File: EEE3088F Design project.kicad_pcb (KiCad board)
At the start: 2 copper layers, 2 parts, among them U7 INA219AxD

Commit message: added circuits
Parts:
- added R9: 1206W4F1002T5E, Resistor_SMD:R_1206_3216Metric_Pad1.30x1.75mm_HandSolder, F.Cu at (148.4, 91.5)

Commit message: saved PCB
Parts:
- added C8: 1uF, Capacitor_SMD:C_1206_3216Metric_Pad1.33x1.80mm_HandSolder, F.Cu at (120.9, 124.9)
- added C9: 1uF, Capacitor_SMD:C_1206_3216Metric_Pad1.33x1.80mm_HandSolder, F.Cu at (129.3, 109.5)
- added D1: D_Schottky, Diode_SMD:D_SOD-123, F.Cu at (126.8, 124.9)
- added D2: D_Schottky, Diode_SMD:D_SOD-123, F.Cu at (129.3, 112.9)
- added L1: 22uH, Inductor_SMD:L_0603_1608Metric_Pad1.05x0.95mm_HandSolder, F.Cu at (126.1, 127.8)
- added L2: 22uH, Inductor_SMD:L_0603_1608Metric_Pad1.05x0.95mm_HandSolder, F.Cu at (120.1, 113.4)
- added L3: 47uH, Inductor_SMD:L_0805_2012Metric_Pad1.05x1.20mm_HandSolder, F.Cu at (133.5, 100.4)
- added Q1: NMOS, Package_TO_SOT_SMD:SOT-23, F.Cu at (133.5, 104.1)
- added R10: 1.1k, Resistor_SMD:R_1206_3216Metric_Pad1.30x1.75mm_HandSolder, F.Cu at (140.9, 100.6)
- added R11: 68, Resistor_SMD:R_1206_3216Metric_Pad1.30x1.75mm_HandSolder, F.Cu at (140.9, 103.9)
- added R12: 1.1k, Resistor_SMD:R_1206_3216Metric_Pad1.30x1.75mm_HandSolder, F.Cu at (140.9, 107.2)
- added R13: 68, Resistor_SMD:R_1206_3216Metric_Pad1.30x1.75mm_HandSolder, F.Cu at (140.9, 110.5)
- added R14: 5.1k, Resistor_SMD:R_0805_2012Metric_Pad1.20x1.40mm_HandSolder, F.Cu at (128.7, 100.5)
- added R15: 390, Resistor_SMD:R_0805_2012Metric_Pad1.20x1.40mm_HandSolder, F.Cu at (128.7, 103.4)
- added R16: 2.7k, Resistor_SMD:R_0805_2012Metric_Pad1.20x1.40mm_HandSolder, F.Cu at (128.7, 106.4)
- added U4: XL1509-3.3, Package_SO:SOIC-8_3.9x4.9mm_P1.27mm, F.Cu at (122.1, 120.0)
- added U7: XL1509-5.0, Package_SO:SOIC-8_3.9x4.9mm_P1.27mm, F.Cu at (122.1, 102.3)
- added U8: TP4056-42-ESOP8, Package_SO:SOIC-8-1EP_3.9x4.9mm_P1.27mm_EP2.41x3.3mm_ThermalVias, F.Cu at (122.1, 108.9)

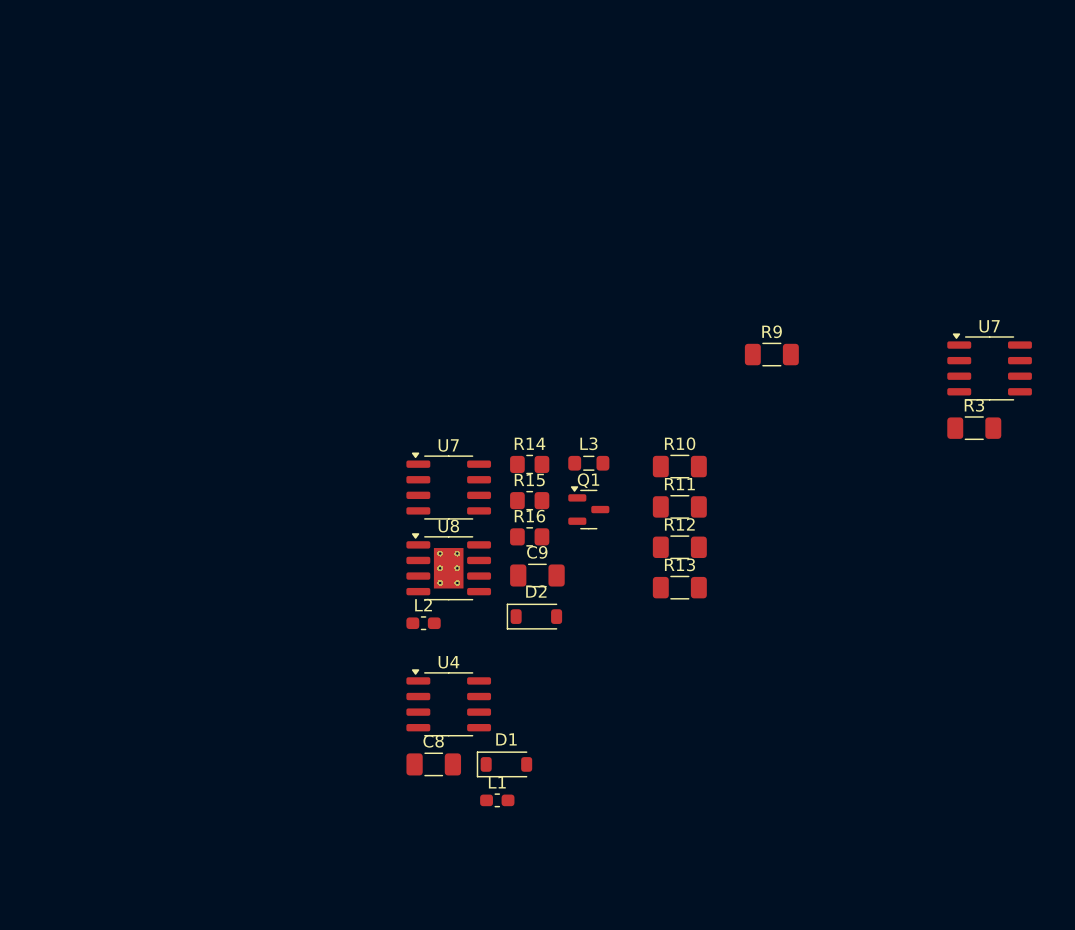
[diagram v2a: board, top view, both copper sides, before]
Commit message: added LCSC numbers and finsihed footprints
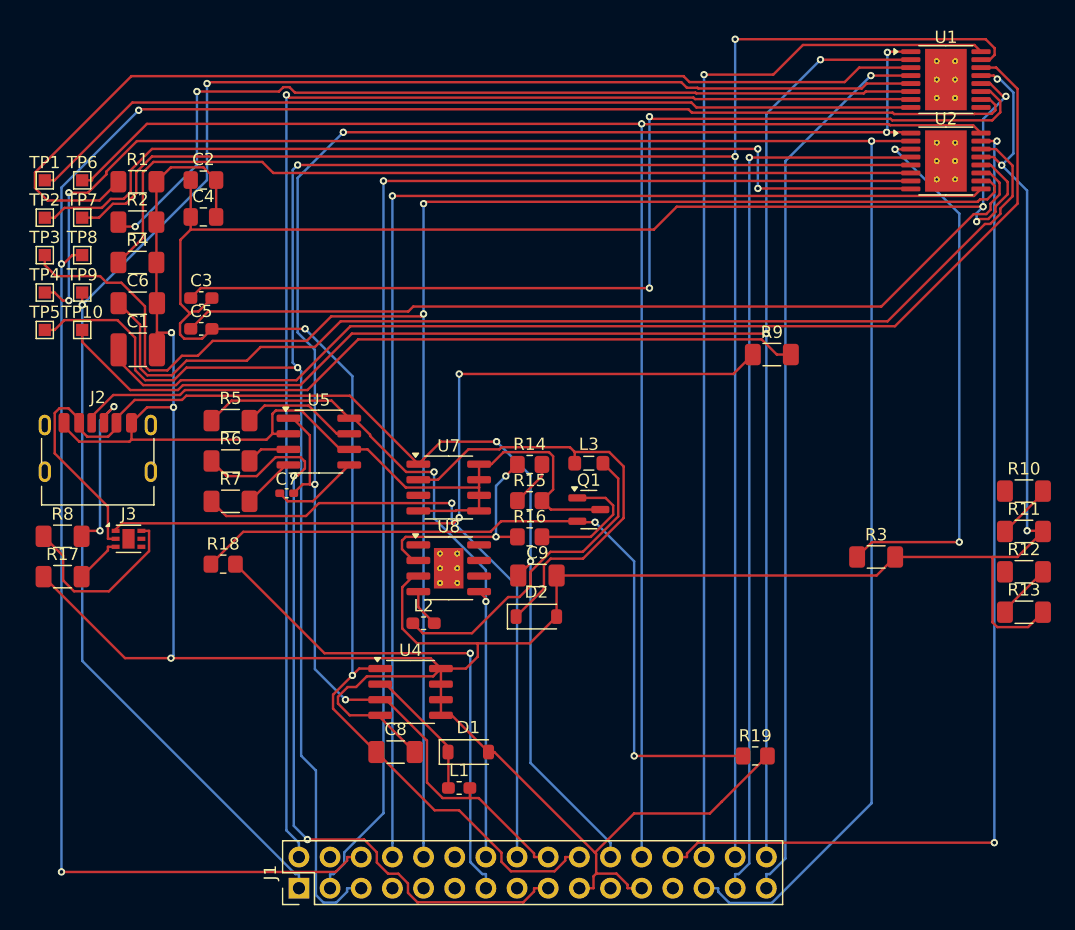
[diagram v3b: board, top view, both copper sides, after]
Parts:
- removed the U7 at (166.2, 92.6)
- added C1: 2.2μ, Capacitor_SMD:C_1210_3225Metric_Pad1.33x2.70mm_HandSolder, F.Cu at (96.8, 91.1)
- added C2: 10μ, Capacitor_SMD:C_0805_2012Metric_Pad1.18x1.45mm_HandSolder, F.Cu at (102.1, 77.3)
- added C3: 10n, Capacitor_SMD:C_0603_1608Metric_Pad1.08x0.95mm_HandSolder, F.Cu at (101.9, 86.9)
- added C4: 10μ, Capacitor_SMD:C_0805_2012Metric_Pad1.18x1.45mm_HandSolder, F.Cu at (102.1, 80.3)
- added C5: 10n, Capacitor_SMD:C_0603_1608Metric_Pad1.08x0.95mm_HandSolder, F.Cu at (101.9, 89.4)
- added C6: 2.2μ, Capacitor_SMD:C_1206_3216Metric_Pad1.33x1.80mm_HandSolder, F.Cu at (96.8, 87.3)
- added C7: 100n, Capacitor_SMD:C_0402_1005Metric_Pad0.74x0.62mm_HandSolder, F.Cu at (108.9, 102.8)
- added J1: Conn_02x16_Odd_Even, Connector_PinHeader_2.54mm:PinHeader_2x16_P2.54mm_Vertical, F.Cu at (109.9, 135.0)
- added J2: 54-00285, Connector_USB:USB_C_Receptacle_HRO_TYPE-C-31-M-17, F.Cu at (93.5, 100.2)
- added J3: HUSB237, Package_DFN_QFN:DFN-6-1EP_2x2mm_P0.65mm_EP1x1.6mm, F.Cu at (96.0, 106.5)
- added R1: 1, Resistor_SMD:R_1206_3216Metric_Pad1.30x1.75mm_HandSolder, F.Cu at (96.7, 77.4)
- added R17: 75k, Resistor_SMD:R_1206_3216Metric_Pad1.30x1.75mm_HandSolder, F.Cu at (90.6, 109.6)
- added R18: 1k, Resistor_SMD:R_0805_2012Metric_Pad1.20x1.40mm_HandSolder, F.Cu at (103.7, 108.6)
- added R19: 10k, Resistor_SMD:R_0805_2012Metric_Pad1.20x1.40mm_HandSolder, F.Cu at (147.1, 124.2)
- added R2: 1, Resistor_SMD:R_1206_3216Metric_Pad1.30x1.75mm_HandSolder, F.Cu at (96.7, 80.7)
- added R4: 0.4, Resistor_SMD:R_1206_3216Metric_Pad1.30x1.75mm_HandSolder, F.Cu at (96.7, 84.0)
- added R5: 0.05, Resistor_SMD:R_1206_3216Metric_Pad1.30x1.75mm_HandSolder, F.Cu at (104.3, 96.9)
- added R6: 10k, Resistor_SMD:R_1206_3216Metric_Pad1.30x1.75mm_HandSolder, F.Cu at (104.3, 100.2)
- added R7: 10k, Resistor_SMD:R_1206_3216Metric_Pad1.30x1.75mm_HandSolder, F.Cu at (104.3, 103.5)
- added R8: 10k, Resistor_SMD:R_1206_3216Metric_Pad1.30x1.75mm_HandSolder, F.Cu at (90.6, 106.3)
- added TP1: TestPoint, TestPoint:TestPoint_Pad_1.0x1.0mm, F.Cu at (89.2, 77.3)
- added TP10: TestPoint, TestPoint:TestPoint_Pad_1.0x1.0mm, F.Cu at (92.2, 89.5)
- added TP2: TestPoint, TestPoint:TestPoint_Pad_1.0x1.0mm, F.Cu at (89.2, 80.3)
- added TP3: TestPoint, TestPoint:TestPoint_Pad_1.0x1.0mm, F.Cu at (89.2, 83.4)
- added TP4: TestPoint, TestPoint:TestPoint_Pad_1.0x1.0mm, F.Cu at (89.2, 86.4)
- added TP5: TestPoint, TestPoint:TestPoint_Pad_1.0x1.0mm, F.Cu at (89.2, 89.5)
- added TP6: TestPoint, TestPoint:TestPoint_Pad_1.0x1.0mm, F.Cu at (92.2, 77.3)
- added TP7: TestPoint, TestPoint:TestPoint_Pad_1.0x1.0mm, F.Cu at (92.2, 80.3)
- added TP8: TestPoint, TestPoint:TestPoint_Pad_1.0x1.0mm, F.Cu at (92.2, 83.4)
- added TP9: TestPoint, TestPoint:TestPoint_Pad_1.0x1.0mm, F.Cu at (92.2, 86.4)
- added U1: Primary motors, Package_SO:HTSSOP-16-1EP_4.4x5mm_P0.65mm_EP3.4x5mm_Mask2.46x2.31mm_ThermalVias, F.Cu at (162.6, 69.1)
- added U2: auxilliary motors, Package_SO:HTSSOP-16-1EP_4.4x5mm_P0.65mm_EP3.4x5mm_Mask2.46x2.31mm_ThermalVias, F.Cu at (162.6, 75.7)
- added U5: INA219AIDR, Package_SO:SOIC-8_3.9x4.9mm_P1.27mm, F.Cu at (111.5, 98.6)
- R9: value 1206W4F1002T5E -> 10k
- moved R10 28.1 mm to (169.0, 102.6)
- moved R11 28.1 mm to (169.0, 105.9)
- moved R12 28.1 mm to (169.0, 109.2)
- moved R13 28.1 mm to (169.0, 112.5)
- moved R3 13.2 mm to (156.9, 108.0)
- moved L1 3.27 mm to (123.0, 126.8)
- moved U4 3.27 mm to (119.0, 119.0)
- moved C8 3.27 mm to (117.8, 123.9)
- moved D1 3.27 mm to (123.7, 123.9)
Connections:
- Q1 pad 2: unconnected-(Q1-G-Pad2) -> Net-(Q1-G)
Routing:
- net GND: track 0.00 -> 342.6 mm, vias 0 -> 6
- net 5V_Out: track 0.00 -> 175.4 mm, vias 0 -> 5
- net MOTOR2_CTRL2: track 0.00 -> 163.7 mm, vias 0 -> 3
- net MOTOR3_A_OUT: track 0.00 -> 153.2 mm, vias 0 -> 3
- net MOTOR1_CTRL2: track 0.00 -> 146.2 mm, vias 0 -> 2
- net MOTOR4_CTRL2: track 0.00 -> 142.0 mm, vias 0 -> 2
- net MOTOR4_B_OUT: track 0.00 -> 140.0 mm, vias 0 -> 2
- net 3V3_Out: track 0.00 -> 137.3 mm, vias 0 -> 5
- net MOTOR2_B_OUT: track 0.00 -> 136.1 mm, vias 0 -> 2
- net MOTOR3_CTRL1: track 0.00 -> 135.3 mm, vias 0 -> 1
- net MOTOR1_A_OUT: track 0.00 -> 134.5 mm, vias 0 -> 2
- net MOTOR2_A_OUT: track 0.00 -> 113.6 mm, vias 0 -> 1
- net MOTOR4_A_OUT: track 0.00 -> 102.6 mm, vias 0 -> 1
- net MOTOR4_CTRL1: track 0.00 -> 102.1 mm, vias 0 -> 1
- net HV: track 0.00 -> 94.5 mm, vias 0 -> 2
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
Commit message: updated pcb
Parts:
- added C12: 100uF, Capacitor_SMD:C_1206_3216Metric_Pad1.33x1.80mm_HandSolder, F.Cu at (194.8, 71.5)
- added C13: 100uF, Capacitor_SMD:C_1206_3216Metric_Pad1.33x1.80mm_HandSolder, F.Cu at (194.8, 74.9)
- added C14: 100uF, Capacitor_SMD:C_1206_3216Metric_Pad1.33x1.80mm_HandSolder, F.Cu at (194.8, 78.2)
- added C15: 100uF, Capacitor_SMD:C_1206_3216Metric_Pad1.33x1.80mm_HandSolder, F.Cu at (194.8, 81.6)
- added C16: 100uF, Capacitor_SMD:C_1206_3216Metric_Pad1.33x1.80mm_HandSolder, F.Cu at (194.8, 85.0)
- added C17: 100uF, Capacitor_SMD:C_1206_3216Metric_Pad1.33x1.80mm_HandSolder, F.Cu at (211.9, 71.5)
- added C18: 100uF, Capacitor_SMD:C_1206_3216Metric_Pad1.33x1.80mm_HandSolder, F.Cu at (211.9, 74.9)
- added C19: 100uF, Capacitor_SMD:C_1206_3216Metric_Pad1.33x1.80mm_HandSolder, F.Cu at (211.9, 78.2)
- added C20: 100uF, Capacitor_SMD:C_1206_3216Metric_Pad1.33x1.80mm_HandSolder, F.Cu at (211.9, 81.6)
- added C21: 100uF, Capacitor_SMD:C_1206_3216Metric_Pad1.33x1.80mm_HandSolder, F.Cu at (211.9, 85.0)
- added C22: 100uF, Capacitor_SMD:C_1206_3216Metric_Pad1.33x1.80mm_HandSolder, F.Cu at (211.9, 88.3)
- added C23: 10uF, Capacitor_SMD:C_0805_2012Metric_Pad1.18x1.45mm_HandSolder, F.Cu at (200.2, 83.9)
- added C24: 100uF, Capacitor_SMD:C_1206_3216Metric_Pad1.33x1.80mm_HandSolder, F.Cu at (211.9, 91.7)
- added C25: 100uF, Capacitor_SMD:C_1206_3216Metric_Pad1.33x1.80mm_HandSolder, F.Cu at (211.9, 95.0)
- added C26: 0.1uF, Capacitor_SMD:C_0402_1005Metric_Pad0.74x0.62mm_HandSolder, F.Cu at (204.3, 95.5)
- added C29: 22uF, Capacitor_SMD:C_0805_2012Metric_Pad1.18x1.45mm_HandSolder, F.Cu at (200.2, 86.9)
- added C30: 22uF, Capacitor_SMD:C_0805_2012Metric_Pad1.18x1.45mm_HandSolder, F.Cu at (200.2, 90.0)
- added C31: 22uF, Capacitor_SMD:C_0805_2012Metric_Pad1.18x1.45mm_HandSolder, F.Cu at (200.2, 93.0)
- added C33: 1nF, Capacitor_SMD:C_0603_1608Metric_Pad1.08x0.95mm_HandSolder, F.Cu at (200.0, 71.1)
- added C35: 47nF, Capacitor_SMD:C_0603_1608Metric_Pad1.08x0.95mm_HandSolder, F.Cu at (200.0, 73.6)
- added C36: 100uF, Capacitor_SMD:C_1206_3216Metric_Pad1.33x1.80mm_HandSolder, F.Cu at (194.8, 88.3)
- added C37: 100uF, Capacitor_SMD:C_1206_3216Metric_Pad1.33x1.80mm_HandSolder, F.Cu at (194.8, 91.7)
- added C38: 100uF, Capacitor_SMD:C_1206_3216Metric_Pad1.33x1.80mm_HandSolder, F.Cu at (194.8, 95.0)
- added C39: 100uF, Capacitor_SMD:C_1206_3216Metric_Pad1.33x1.80mm_HandSolder, F.Cu at (194.8, 98.3)
- added L5: 1.2uH, Inductor_SMD:L_0805_2012Metric_Pad1.05x1.20mm_HandSolder, F.Cu at (200.3, 95.8)
- added R11: 2.2k, Resistor_SMD:R_0603_1608Metric_Pad0.98x0.95mm_HandSolder, F.Cu at (219.1, 71.1)
- added R12: 2.2k, Resistor_SMD:R_0603_1608Metric_Pad0.98x0.95mm_HandSolder, F.Cu at (219.1, 73.6)
- added R13: 2.2k, Resistor_SMD:R_0603_1608Metric_Pad0.98x0.95mm_HandSolder, F.Cu at (219.1, 76.2)
- added R20: 33K, Resistor_SMD:R_0603_1608Metric_Pad0.98x0.95mm_HandSolder, F.Cu at (200.0, 76.2)
- added R22: 220K, Resistor_SMD:R_0603_1608Metric_Pad0.98x0.95mm_HandSolder, F.Cu at (200.0, 78.7)
- added R23: 68K, Resistor_SMD:R_0603_1608Metric_Pad0.98x0.95mm_HandSolder, F.Cu at (200.0, 81.2)
- added R24: 100K, Resistor_SMD:R_0402_1005Metric_Pad0.72x0.64mm_HandSolder, F.Cu at (199.5, 98.2)
- added R25: 150K, Resistor_SMD:R_0805_2012Metric_Pad1.20x1.40mm_HandSolder, F.Cu at (204.6, 71.3)
- added R26: 47K, Resistor_SMD:R_0805_2012Metric_Pad1.20x1.40mm_HandSolder, F.Cu at (204.6, 74.3)
- R10: value 1.1k -> 2.2k; footprint Resistor_SMD:R_1206_3216Metric_Pad1.30x1.75mm_HandSolder -> Resistor_SMD:R_0603_1608Metric_Pad0.98x0.95mm_HandSolder
- R15, R18: footprint Resistor_SMD:R_0805_2012Metric_Pad1.20x1.40mm_HandSolder -> Resistor_SMD:R_0603_1608Metric_Pad0.98x0.95mm_HandSolder
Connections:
- net Net-(U5-VIN-) renamed VCC
- L2 pad 1: Net-(L2-Pad1) -> Net-(D2-K)
- R10 pad 2: Net-(R10-Pad2) -> GND

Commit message: Removed old backups and update KiCad files
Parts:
- added J4: Conn_01x02, Connector_JST:JST_PH_S2B-PH-K_1x02_P2.00mm_Horizontal, F.Cu at (199.9, 134.7)
- added SW1: SW_SPDT, SWITCH:Untitled, F.Cu at (72.6, 48.7)
- added TP11: TestPoint, TestPoint:TestPoint_Pad_1.0x1.0mm, F.Cu at (198.4, 145.4)
- added TP12: TestPoint, TestPoint:TestPoint_Pad_1.0x1.0mm, F.Cu at (198.4, 148.5)
- added TP13: TestPoint, TestPoint:TestPoint_Pad_1.0x1.0mm, F.Cu at (193.4, 133.8)
- added TP14: TestPoint, TestPoint:TestPoint_Pad_1.0x1.0mm, F.Cu at (193.4, 136.8)
- added TP15: TestPoint, TestPoint:TestPoint_Pad_1.0x1.0mm, F.Cu at (193.4, 139.9)
- added TP16: TestPoint, TestPoint:TestPoint_Pad_1.0x1.0mm, F.Cu at (193.4, 142.9)
- added TP17: TestPoint, TestPoint:TestPoint_Pad_1.0x1.0mm, F.Cu at (203.5, 145.4)
- added TP18: TestPoint, TestPoint:TestPoint_Pad_1.0x1.0mm, F.Cu at (203.5, 148.5)
- added U3: TPS22950YBHR, TPS22950YBHR:IC_TPS22950YBHR, F.Cu at (67.5, 63.6)
- added U6: TPS22950YBHR, TPS22950YBHR:IC_TPS22950YBHR, F.Cu at (71.3, 63.6)
- added U9: TPS61088RHLR, TPS61088RHLR:IC_TPS61088RHLR, F.Cu at (68.4, 56.3)
- U8: footprint Package_SO:SOIC-8-1EP_3.9x4.9mm_P1.27mm_EP2.41x3.3mm_ThermalVias -> TP4056-42-ESOP8:SOIC127P600X175-9N
